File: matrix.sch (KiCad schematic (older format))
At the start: 180 parts, among them SW1 SW_Push, SW10 SW_Push, SW11 SW_Push, SW12 SW_Push, SW13 SW_Push, SW14 SW_Push, SW15 SW_Push, SW16 SW_Push, SW17 SW_Push, SW18 SW_Push, SW19 SW_Push, SW2 SW_Push, SW20 SW_Push, SW21 SW_Push, SW22 SW_Push, SW23 SW_Push, SW24 SW_Push, SW25 SW_Push, SW26 SW_Push, SW27 SW_Push, SW28 SW_Push, SW29 SW_Push, SW3 SW_Push, SW30 SW_Push, SW31 SW_Push, SW32 SW_Push, SW33 SW_Push, SW34 SW_Push, SW35 SW_Push, SW36 SW_Push, SW37 SW_Push, SW38 SW_Push, SW39 SW_Push, SW4 SW_Push, SW40 SW_Push, SW41 SW_Push, SW42 SW_Push, SW43 SW_Push, SW44 SW_Push, SW45 SW_Push, SW46 SW_Push, SW47 SW_Push, SW48 SW_Push, SW49 SW_Push, SW5 SW_Push, SW50 SW_Push, SW51 SW_Push, SW52 SW_Push, SW53 SW_Push, SW54 SW_Push, SW55 SW_Push, SW56 SW_Push, SW57 SW_Push, SW58 SW_Push, SW59 SW_Push, SW6 SW_Push, SW60 SW_Push, SW61 SW_Push, SW62 SW_Push, SW63 SW_Push, SW64 SW_Push, SW65 SW_Push, SW66 SW_Push, SW67 SW_Push, SW68 SW_Push, SW69 SW_Push, SW7 SW_Push, SW70 SW_Push, SW71 SW_Push, SW72 SW_Push, SW73 SW_Push, SW74 SW_Push, SW75 SW_Push, SW76 SW_Push, SW77 SW_Push, SW78 SW_Push, SW79 SW_Push, SW8 SW_Push, SW80 SW_Push, SW81 SW_Push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

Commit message: v1d
:skull: you do not want to know.
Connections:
- wire segments 190 -> 198
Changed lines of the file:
@@
 	0    -1   -1   0
 $EndComp
-Wire Wire Line
-	2150 1950 2150 1650
 Connection ~ 2150 1950
 Wire Wire Line
@@
 	0    -1   -1   0
 $EndComp
-Wire Wire Line
-	2650 1950 2650 1650
 Connection ~ 2650 1950
 Wire Wire Line
@@
 	0    -1   -1   0
 $EndComp
-Wire Wire Line
-	3150 1950 3150 1650
 Connection ~ 3150 1950
 Wire Wire Line
@@
 	0    -1   -1   0
 $EndComp
-Wire Wire Line
-	3650 1950 3650 1650
 Connection ~ 3650 1950
 Wire Wire Line
@@
 	0    -1   -1   0
 $EndComp
-Wire Wire Line
-	4150 1950 4150 1650
 Connection ~ 4150 1950
 Wire Wire Line
@@
 	0    -1   -1   0
 $EndComp
-Wire Wire Line
-	4650 1950 4650 1650
 Connection ~ 4650 1950
 Wire Wire Line
@@
 	0    -1   -1   0
 $EndComp
-Wire Wire Line
-	5150 1950 5150 1650
 Connection ~ 5150 1950
 Wire Wire Line
@@
 	0    -1   -1   0
 $EndComp
-Wire Wire Line
-	5650 1950 5650 1650
 Connection ~ 5650 1950
 Wire Wire Line
@@
 	0    -1   -1   0
 $EndComp
-Wire Wire Line
-	6150 1950 6150 1650
 Connection ~ 6150 1950
 Wire Wire Line
@@
 	0    -1   -1   0
 $EndComp
-Wire Wire Line
-	6650 1950 6650 1650
 Connection ~ 6650 1950
 Wire Wire Line
@@
 	0    -1   -1   0
 $EndComp
-Wire Wire Line
-	7150 1950 7150 1650
 Connection ~ 7150 1950
 Wire Wire Line
@@
 	0    -1   -1   0
 $EndComp
-Wire Wire Line
-	7650 1950 7650 1650
 Connection ~ 7650 1950
 Wire Wire Line
@@
 	0    -1   -1   0
 $EndComp
-Wire Wire Line
-	8150 1950 8150 1650
 Connection ~ 8150 1950
 Wire Wire Line
@@
 	0    -1   -1   0
 $EndComp
-Wire Wire Line
-	8650 1950 8650 1650
 Connection ~ 8250 2150
 $Comp
@@
 Connection ~ 9250 2150
 Connection ~ 9650 1950
-Wire Wire Line
-	9650 1950 9650 1650
 $Comp
 L Device:D_Small D16
@@
 	8750 2150 9250 2150
 Connection ~ 9150 1950
-Wire Wire Line
-	9150 1950 9150 1650
 $Comp
 L Switch:SW_Push SW15
@@
 Connection ~ 9750 2150
 Connection ~ 10150 1950
-Wire Wire Line
-	10150 1950 10150 1650
 $Comp
 L Device:D_Small D17
@@
 Text GLabel 10150 1350 1    50   Input ~ 0
 col16
+Wire Wire Line
+	1550 2150 1750 2150
+Connection ~ 1750 2150
+Wire Wire Line
+	2150 1350 2150 1950
+Wire Wire Line
+	2650 1350 2650 1950
+Wire Wire Line
+	3150 1350 3150 1950
+Wire Wire Line
+	3650 1350 3650 1950
+Wire Wire Line
+	4150 1350 4150 1950
+Wire Wire Line
+	4650 1350 4650 1950
+Wire Wire Line
+	5150 1350 5150 1950
+Wire Wire Line
+	1550 2750 1750 2750
+Connection ~ 1750 2750
+Wire Wire Line
+	1550 3350 1750 3350
+Connection ~ 1750 3350
+Wire Wire Line
+	1550 3950 1750 3950
+Connection ~ 1750 3950
+Wire Wire Line
+	1550 4500 1650 4500
+Wire Wire Line
+	1650 4500 1650 4550
+Wire Wire Line
+	1650 4550 1750 4550
+Connection ~ 1750 4550
+Wire Wire Line
+	1550 5150 1750 5150
+Connection ~ 1750 5150
+Wire Wire Line
+	5650 1350 5650 1950
+Wire Wire Line
+	6150 1350 6150 1950
+Wire Wire Line
+	6650 1350 6650 1950
+Wire Wire Line
+	7150 1350 7150 1950
+Wire Wire Line
+	7650 1350 7650 1950
+Wire Wire Line
+	8150 1350 8150 1950
+Wire Wire Line
+	8650 1350 8650 1950
+Wire Wire Line
+	9150 1350 9150 1950
+Wire Wire Line
+	9650 1350 9650 1950
+Wire Wire Line
+	10150 1350 10150 1950
 $EndSCHEMATC

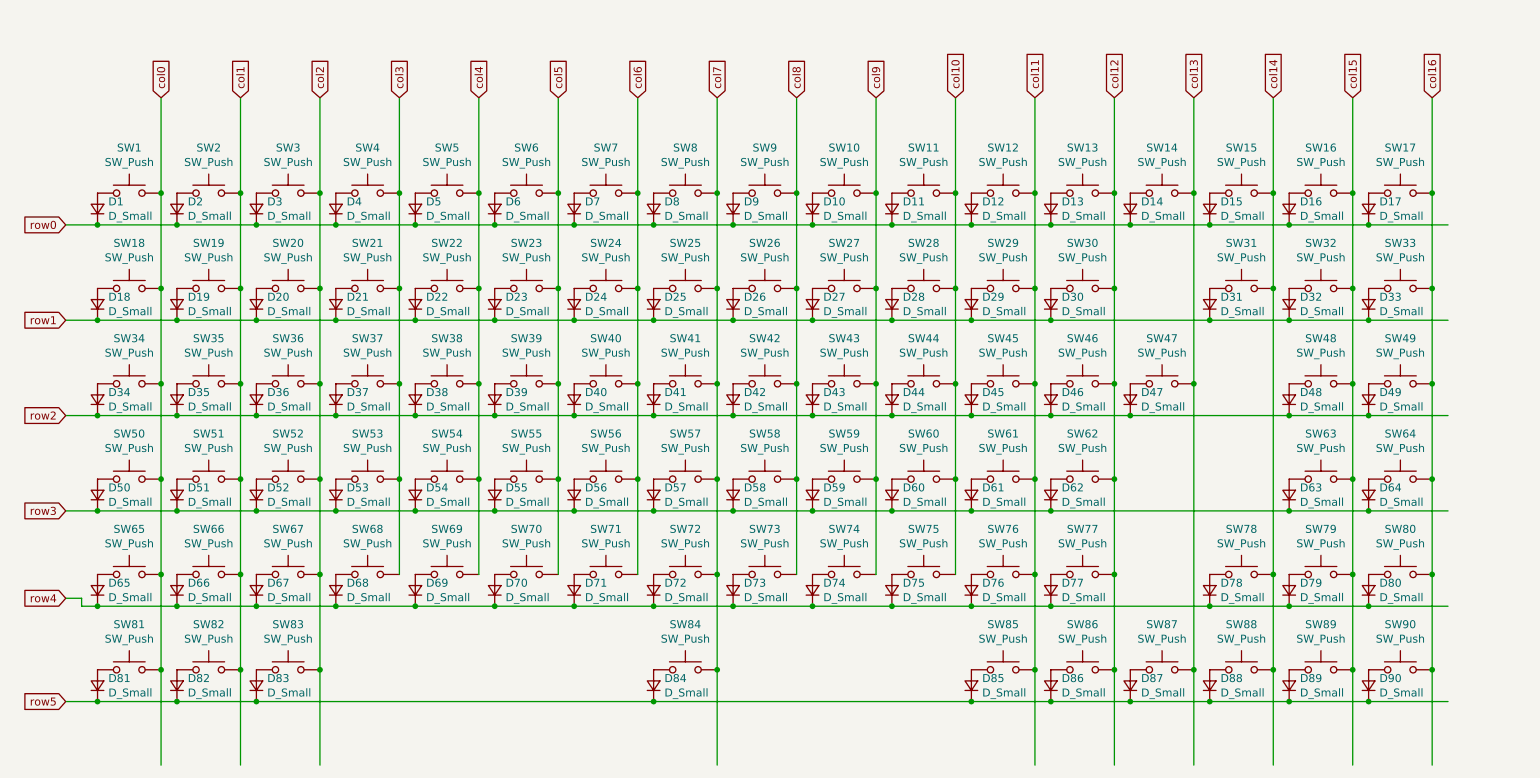
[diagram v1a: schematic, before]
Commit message: v1c2
Redid switch matrix, AGAIN.
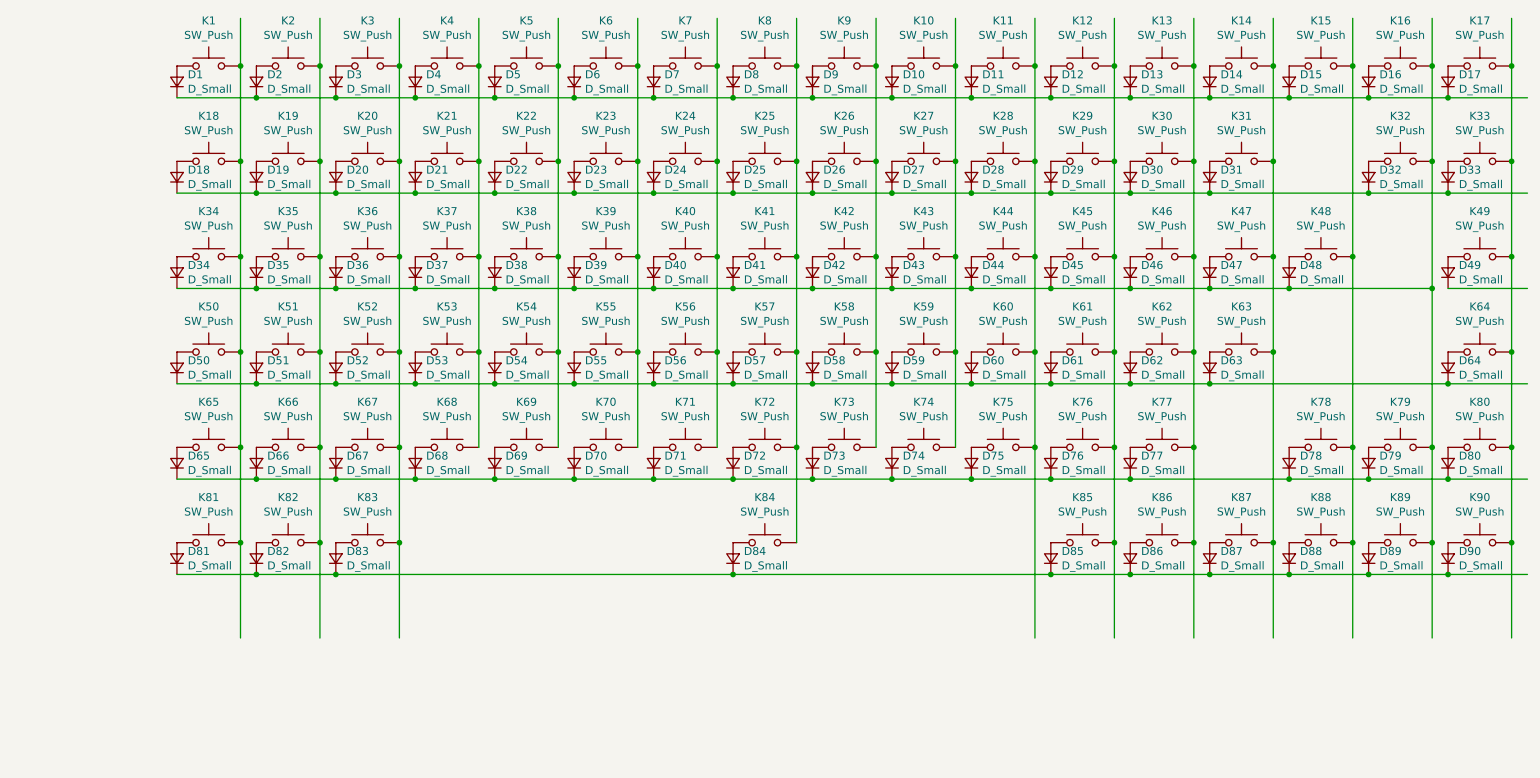
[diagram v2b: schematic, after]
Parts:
- removed SW1, SW10, SW11, SW12, SW13, SW14, SW15, SW16, SW17, SW18, SW19, SW2, SW20, SW21, SW22, SW23, SW24, SW25, SW26, SW27, SW28, SW29, SW3, SW30, SW31, SW32, SW33, SW34, SW35, SW36, SW37, SW38, SW39, SW4, SW40, SW41, SW42, SW43, SW44, SW45, SW46, SW47, SW48, SW49, SW5, SW50, SW51, SW52, SW53, SW54, SW55, SW56, SW57, SW58, SW59, SW6, SW60, SW61, SW62, SW63, SW64, SW65, SW66, SW67, SW68, SW69, SW7, SW70, SW71, SW72, SW73, SW74, SW75, SW76, SW77, SW78, SW79, SW8, SW80, SW81, SW82, SW83, SW84, SW85, SW86, SW87, SW88, SW89, SW9, SW90: SW_Push, symbol Switch:SW_Push
- added K1, K10, K11, K12, K13, K14, K15, K16, K17, K18, K19, K2, K20, K21, K22, K23, K24, K25, K26, K27, K28, K29, K3, K30, K31, K32, K33, K34, K35, K36, K37, K38, K39, K4, K40, K41, K42, K43, K44, K45, K46, K47, K48, K49, K5, K50, K51, K52, K53, K54, K55, K56, K57, K58, K59, K6, K60, K61, K62, K63, K64, K65, K66, K67, K68, K69, K7, K70, K71, K72, K73, K74, K75, K76, K77, K78, K79, K8, K80, K81, K82, K83, K84, K85, K86, K87, K88, K89, K9, K90: SW_Push, symbol Switch:SW_Push
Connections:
- net labels removed: col0, col1, col10, col11, col12, col13, col14, col15, col16, col2, col3, col4, col5, col6, col7, col8, col9, row0, row1, row2, row3, row4, row5
- wire segments 198 -> 191
